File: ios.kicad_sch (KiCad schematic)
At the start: 45 parts, among them Q4 BSS138PW,115, SW1 SW_SKRPABE010, SW2 SW_SKRPABE010, SW3 SW_SKRPABE010, SW4 SW_SKRPABE010, SW8 CVS-04B, U25 74LVC06ABQ

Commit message: Update push button and VEML footprints from lib
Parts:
- SW1, SW2, SW3, SW4: footprint antmicro-footprints:SW_PTS810SJM250SMTRLFS_SMD -> antmicro-footprints:SW_SKRPABE010_SMD
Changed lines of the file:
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@@
 			)
 		)
-		(property "Footprint" "antmicro-footprints:SW_PTS810SJM250SMTRLFS_SMD"
+		(property "Footprint" "antmicro-footprints:SW_SKRPABE010_SMD"
 			(at 368.3 163.83 0)
 			(hide yes)
@@
 			)
 		)
-		(property "Footprint" "antmicro-footprints:SW_PTS810SJM250SMTRLFS_SMD"
+		(property "Footprint" "antmicro-footprints:SW_SKRPABE010_SMD"
 			(at 368.3 134.62 0)
 			(hide yes)
@@
 			)
 		)
-		(property "Footprint" "antmicro-footprints:SW_PTS810SJM250SMTRLFS_SMD"
+		(property "Footprint" "antmicro-footprints:SW_SKRPABE010_SMD"
 			(at 368.3 105.41 0)
 			(hide yes)
@@
 			)
 		)
-		(property "Footprint" "antmicro-footprints:SW_PTS810SJM250SMTRLFS_SMD"
+		(property "Footprint" "antmicro-footprints:SW_SKRPABE010_SMD"
 			(at 368.3 193.04 0)
 			(hide yes)

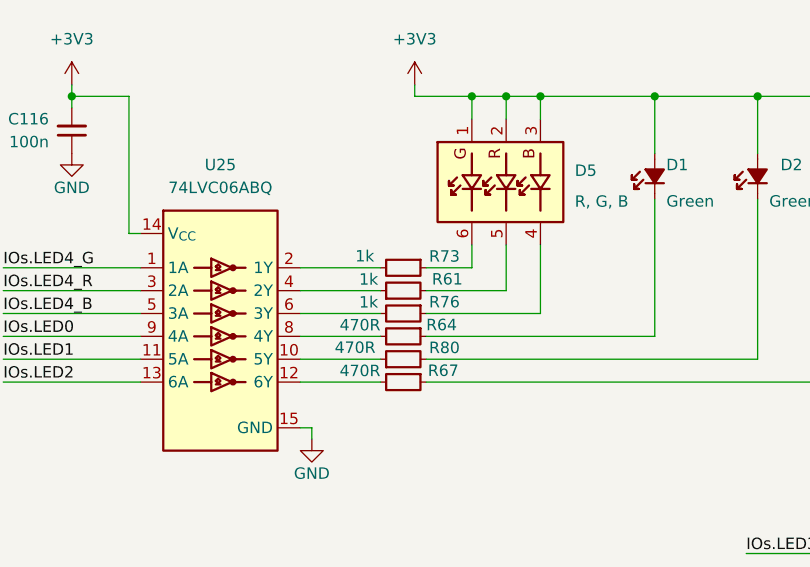
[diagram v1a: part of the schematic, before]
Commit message: [#102004] Change RGB LED resistors in schematic
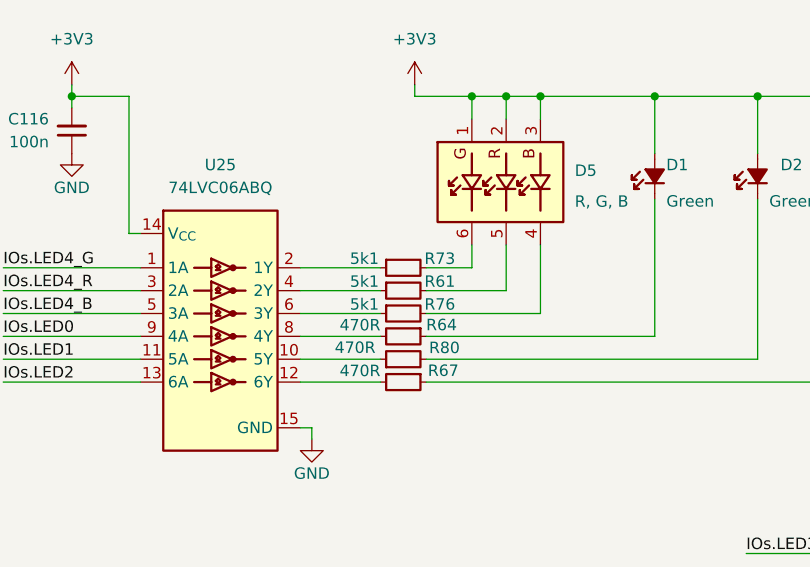
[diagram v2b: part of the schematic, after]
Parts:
- removed R61, R73, R76: R_1k_0402, antmicro-footprints:R_0402_1005Metric, symbol antmicroResistors0402:R_1k_0402
- added R61, R73, R76: R_5k1_0402, antmicro-footprints:R_0402_1005Metric, symbol antmicroResistors0402:R_5k1_0402
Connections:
- net at D5.6 (C_{G}): now also R73.2
- net at U25.2 (1Y): now also R73.1
- net at U25.4 (2Y): now also R61.1
- net at U25.6 (3Y): now also R76.1
- net at D5.4 (C_{B}): now also R76.2
- net at D5.5 (C_{R}): now also R61.2

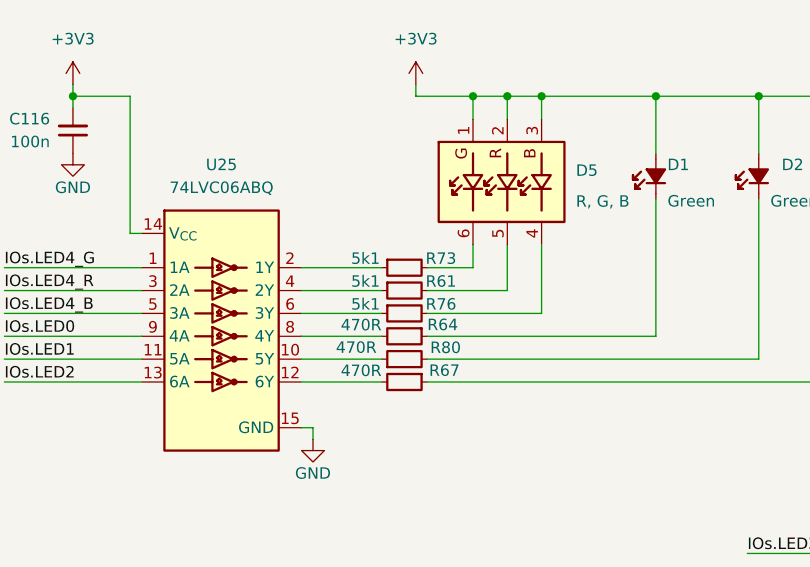
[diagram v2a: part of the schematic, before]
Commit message: [#102004] Change RGB LED resistors - rotate resistors
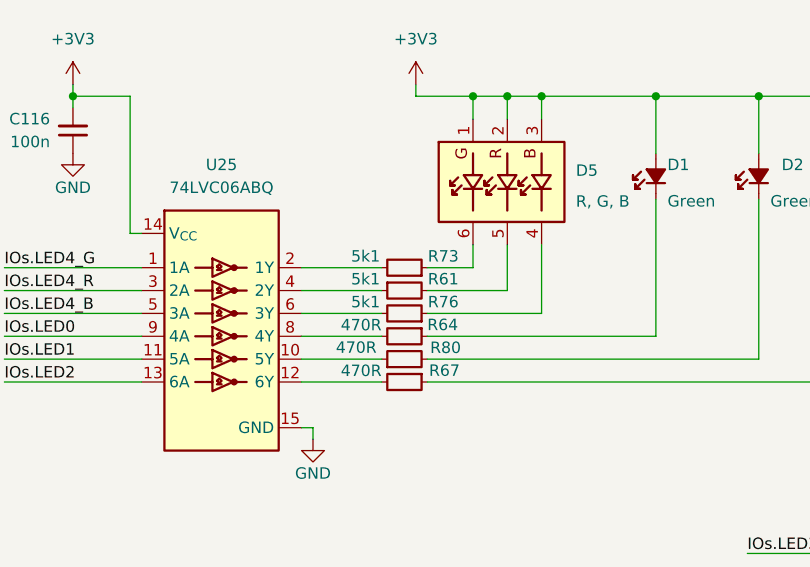
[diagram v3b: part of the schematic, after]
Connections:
- net at R76.1: now also D5.4 (C_{B}); no longer U25.6 (3Y)
- net at R76.2: now also U25.6 (3Y); no longer D5.4 (C_{B})
- net at U25.2 (1Y): now also R73.2; no longer R73.1
- net at D5.6 (C_{G}): now also R73.1; no longer R73.2
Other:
- moved on the sheet: R73, R76
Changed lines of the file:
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@@
 	(title_block
 		(title "STM32H7 Renode Reference Platform")
-		(date "2026-07-30")
+		(date "2026-07-31")
 		(rev "1.1.2")
 		(company "Antmicro")
@@
 	(symbol
 		(lib_id "antmicroResistors0402:R_5k1_0402")
-		(at 146.05 91.44 0)
+		(at 151.13 91.44 180)
 		(unit 1)
 		(body_style 1)
@@
 		(dnp no)
 		(property "Reference" "R76"
-			(at 152.654 90.424 0)
+			(at 152.908 90.17 0)
 			(show_name no)
 			(do_not_autoplace no)
@@
 		)
 		(property "Value" "R_5k1_0402"
-			(at 166.37 104.14 0)
+			(at 130.81 78.74 0)
 			(hide yes)
 			(show_name no)
@@
 		)
 		(property "Footprint" "antmicro-footprints:R_0402_1005Metric"
-			(at 166.37 106.68 0)
+			(at 130.81 76.2 0)
 			(hide yes)
 			(show_name no)
@@
 		)
 		(property "Datasheet" "https://www.bourns.com/docs/product-datasheets/cr.pdf"
-			(at 166.37 109.22 0)
+			(at 130.81 73.66 0)
 			(hide yes)
 			(show_name no)
@@
 		)
 		(property "Description" "SMD Chip Resistor, 5.1 kohm, ± 1%, 63 mW, 0402 [1005 Metric], Thick Film, General Purpose"
-			(at 166.37 121.92 0)
+			(at 130.81 60.96 0)
 			(hide yes)
 			(show_name no)
@@
 		)
 		(property "MPN" "CR0402-FX-5101GLF"
-			(at 166.37 111.76 0)
+			(at 130.81 71.12 0)
 			(hide yes)
 			(show_name no)
@@
 		)
 		(property "Manufacturer" "Bourns"
-			(at 166.37 114.3 0)
+			(at 130.81 68.58 0)
 			(hide yes)
 			(show_name no)
@@
 		)
 		(property "License" "Apache-2.0"
-			(at 166.37 116.84 0)
+			(at 130.81 66.04 0)
 			(hide yes)
 			(show_name no)
@@
 		)
 		(property "Author" "Antmicro"
-			(at 166.37 119.38 0)
+			(at 130.81 63.5 0)
 			(hide yes)
 			(show_name no)
@@
 		)
 		(property "Val" "5k1"
-			(at 144.272 90.424 0)
+			(at 144.272 90.17 0)
 			(show_name no)
 			(do_not_autoplace no)
@@
 		)
 		(property "Tolerance" "1%"
-			(at 166.37 101.6 0)
+			(at 130.81 81.28 0)
 			(hide yes)
 			(show_name no)
@@
 	(symbol
 		(lib_id "antmicroResistors0402:R_5k1_0402")
-		(at 146.05 86.36 0)
+		(at 151.13 86.36 180)
 		(unit 1)
 		(body_style 1)
@@
 		(dnp no)
 		(property "Reference" "R73"
-			(at 152.654 85.344 0)
+			(at 152.908 85.09 0)
 			(show_name no)
 			(do_not_autoplace no)
@@
 		)
 		(property "Value" "R_5k1_0402"
-			(at 166.37 99.06 0)
+			(at 130.81 73.66 0)
 			(hide yes)
 			(show_name no)
@@
 		)
 		(property "Footprint" "antmicro-footprints:R_0402_1005Metric"
-			(at 166.37 101.6 0)
+			(at 130.81 71.12 0)
 			(hide yes)
 			(show_name no)
@@
 		)
 		(property "Datasheet" "https://www.bourns.com/docs/product-datasheets/cr.pdf"
-			(at 166.37 104.14 0)
+			(at 130.81 68.58 0)
 			(hide yes)
 			(show_name no)
@@
 		)
 		(property "Description" "SMD Chip Resistor, 5.1 kohm, ± 1%, 63 mW, 0402 [1005 Metric], Thick Film, General Purpose"
-			(at 166.37 116.84 0)
+			(at 130.81 55.88 0)
 			(hide yes)
 			(show_name no)
@@
 		)
 		(property "MPN" "CR0402-FX-5101GLF"
-			(at 166.37 106.68 0)
+			(at 130.81 66.04 0)
 			(hide yes)
 			(show_name no)
@@
 		)
 		(property "Manufacturer" "Bourns"
-			(at 166.37 109.22 0)
+			(at 130.81 63.5 0)
 			(hide yes)
 			(show_name no)
@@
 		)
 		(property "License" "Apache-2.0"
-			(at 166.37 111.76 0)
+			(at 130.81 60.96 0)
 			(hide yes)
 			(show_name no)
@@
 		)
 		(property "Author" "Antmicro"
-			(at 166.37 114.3 0)
+			(at 130.81 58.42 0)
 			(hide yes)
 			(show_name no)
@@
 		)
 		(property "Val" "5k1"
-			(at 144.272 85.344 0)
+			(at 144.272 85.09 0)
 			(show_name no)
 			(do_not_autoplace no)
@@
 		)
 		(property "Tolerance" "1%"
-			(at 166.37 96.52 0)
+			(at 130.81 76.2 0)
 			(hide yes)
 			(show_name no)
@@
 		(dnp no)
 		(property "Reference" "R61"
-			(at 152.654 87.884 0)
+			(at 152.908 87.63 0)
 			(show_name no)
 			(do_not_autoplace no)
@@
 		)
 		(property "Val" "5k1"
-			(at 144.272 87.884 0)
+			(at 144.272 87.63 0)
 			(show_name no)
 			(do_not_autoplace no)
